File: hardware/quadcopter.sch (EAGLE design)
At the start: 92 parts, among them J1 HEADER-4POS-0.1IN-FEMALE-SMD-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, J2 HEADER-10POSTH-254X10, J3 HEADER-4POS-0.1IN-FEMALE, J4 AVR_SPI_PRG_6-SMD, M1 MOTOR_PADS_GND-MOLEX-SMD, M2 MOTOR_PADS_GND-MOLEX-SMD, M3 MOTOR_PADS_GND-MOLEX-SMD, M4 MOTOR_PADS_GND-MOLEX-SMD, Q1 N-MOSFET-SI2302DS, Q10 N-MOSFET-SI2302DS, Q11 N-MOSFET-SI2302DS, Q12 N-MOSFET-SI2302DS, Q2 N-MOSFET-SI2302DS, Q3 N-MOSFET-SI2302DS, Q4 N-MOSFET-SI2302DS, Q5 N-MOSFET-SI2302DS, Q6 N-MOSFET-SI2302DS, Q7 N-MOSFET-SI2302DS, Q8 N-MOSFET-SI2302DS, Q9 N-MOSFET-SI2302DS, SW1 PUSHBUTTON_-4.5X4.5, U1 ATMEGA128RFA1, U2 IMU_LSM9DS1-LSM9DS1, Y1 CRYSTAL5X3

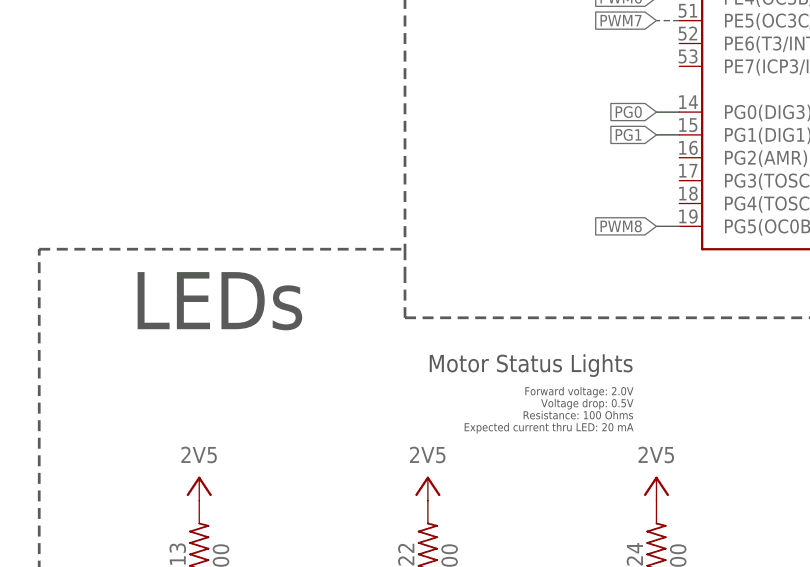
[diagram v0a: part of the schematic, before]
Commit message: Fixed 2V5 net on both sides of R15
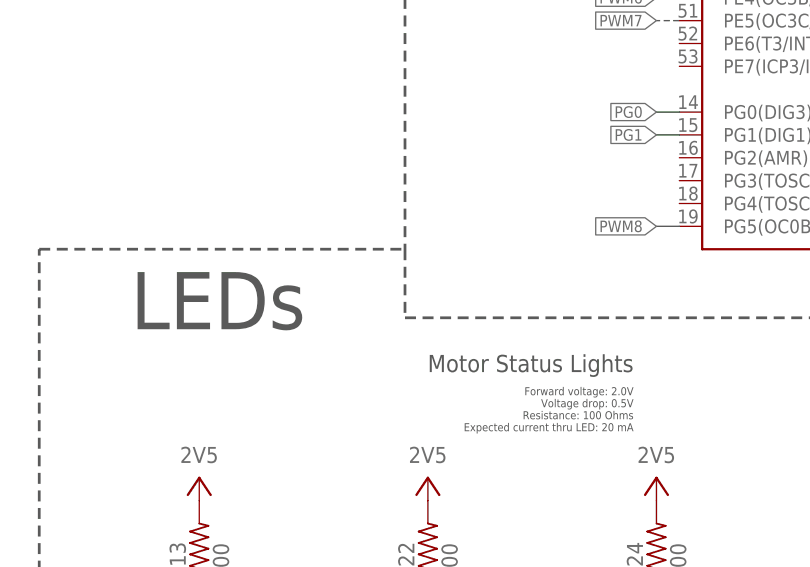
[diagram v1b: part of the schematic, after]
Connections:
- new net N$33: D12.A, R15.1
- net 2V5: no longer D12.A, R15.1
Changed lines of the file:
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@@
 <text x="332.74" y="116.84" size="7.62" layer="97">Power Supply</text>
 <wire x1="154.94" y1="274.32" x2="154.94" y2="137.16" width="0.3048" layer="97" style="longdash"/>
-<wire x1="154.94" y1="134.62" x2="154.94" y2="129.54" width="0.3048" layer="97" style="longdash"/>
+<wire x1="154.94" y1="137.16" x2="154.94" y2="129.54" width="0.3048" layer="97" style="longdash"/>
 <wire x1="154.94" y1="129.54" x2="327.66" y2="129.54" width="0.3048" layer="97" style="longdash"/>
 <text x="205.74" y="261.62" size="7.62" layer="97">Microcontroller</text>
@@
 <wire x1="114.3" y1="58.42" x2="114.3" y2="137.16" width="0.3048" layer="97" style="longdash"/>
 <wire x1="114.3" y1="137.16" x2="154.94" y2="137.16" width="0.3048" layer="97" style="longdash"/>
-<wire x1="154.94" y1="137.16" x2="154.94" y2="134.62" width="0.3048" layer="97" style="longdash"/>
 <wire x1="261.62" y1="60.96" x2="314.96" y2="60.96" width="0.1524" layer="97" style="longdash"/>
 </plain>
@@
 </segment>
 <segment>
-<pinref part="D12" gate="G$1" pin="A"/>
 <pinref part="R15" gate="G$1" pin="2"/>
-<pinref part="R15" gate="G$1" pin="1"/>
 <pinref part="R8" gate="G$1" pin="2"/>
 <wire x1="238.76" y1="111.76" x2="243.84" y2="111.76" width="0.1524" layer="91"/>
@@
 </segment>
 </net>
+<net name="N$33" class="0">
+<segment>
+<pinref part="D12" gate="G$1" pin="A"/>
+<pinref part="R15" gate="G$1" pin="1"/>
+</segment>
+</net>

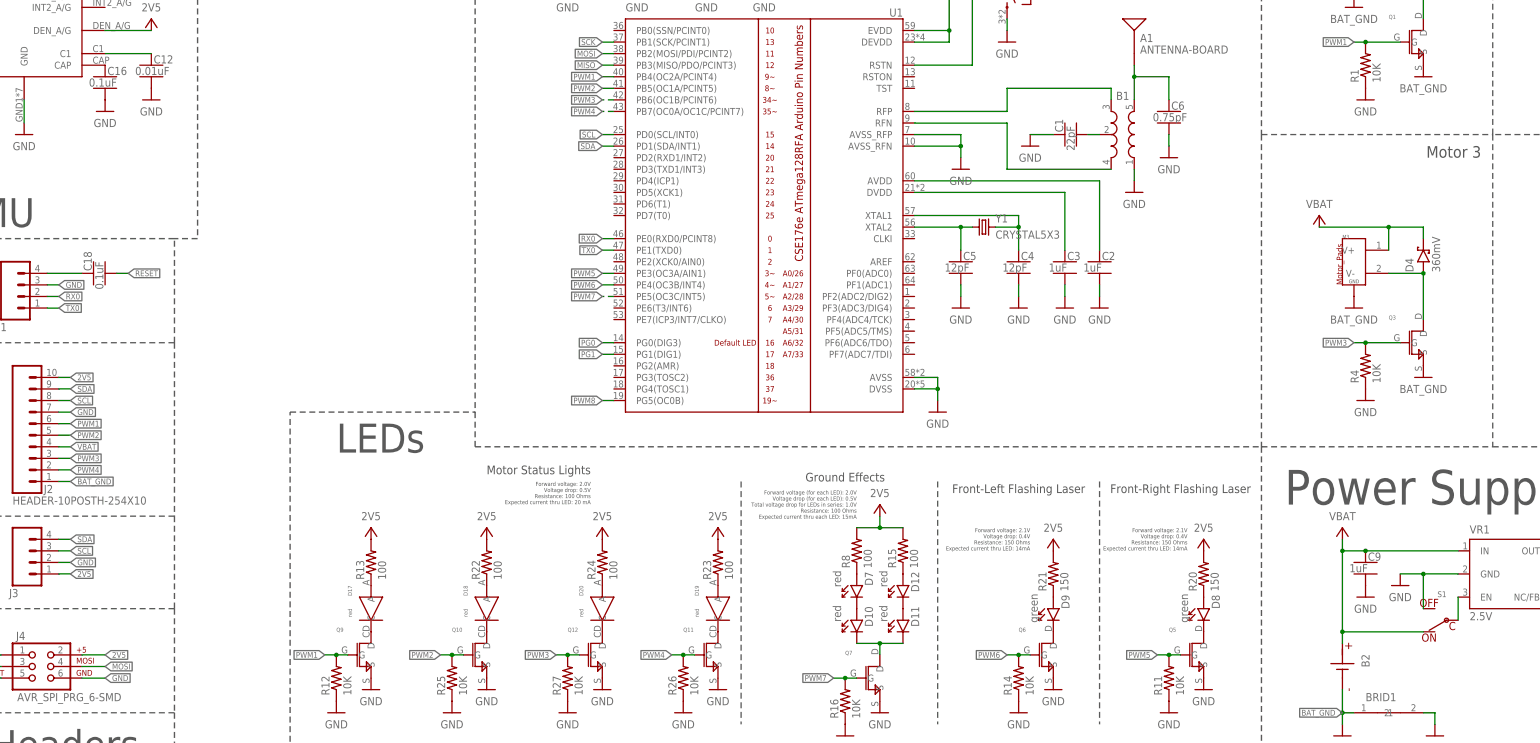
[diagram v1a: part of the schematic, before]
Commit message: Wired some pins to GND and switch to BAT_GND for eaglint
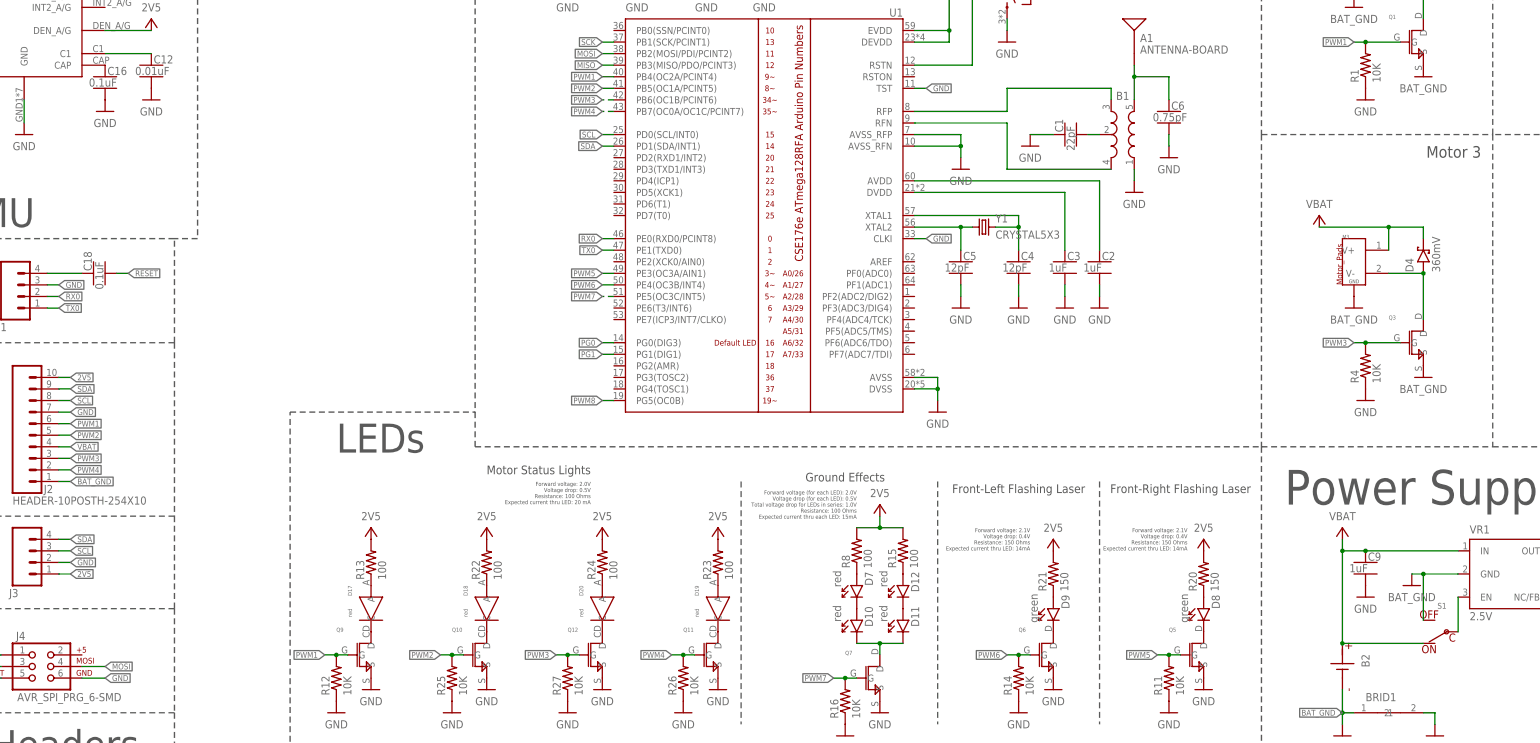
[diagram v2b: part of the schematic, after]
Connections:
- net 2V5: no longer J4.2
- net BAT_GND: now also S1.OFF, VR1.GND
- net GND: now also U1.CLKI, U1.TST; no longer S1.OFF, VR1.GND
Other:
- moved on the sheet: S1
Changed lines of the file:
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@@
 <part name="A1" library="quadparts_prebuilt_2022" library_urn="urn:adsk.wipprod:fs.file:vf.VudH_-qgS-enOFMGlZoxrw" deviceset="ANTENNA" device="-BOARD"/>
 <part name="VR1" library="quadparts_prebuilt_2022" library_urn="urn:adsk.wipprod:fs.file:vf.VudH_-qgS-enOFMGlZoxrw" deviceset="TPS73633-DBVT" device="2.5V" value="2.5V"/>
-<part name="GND27" library="quadparts_prebuilt_2022" library_urn="urn:adsk.wipprod:fs.file:vf.VudH_-qgS-enOFMGlZoxrw" deviceset="GND" device=""/>
 <part name="C9" library="quadparts_prebuilt_2022" library_urn="urn:adsk.wipprod:fs.file:vf.VudH_-qgS-enOFMGlZoxrw" deviceset="CAPACITOR-NP_" device="SMD-2012-0805_CERAMIC-1UF" value="1uF"/>
 <part name="C10" library="quadparts_prebuilt_2022" library_urn="urn:adsk.wipprod:fs.file:vf.VudH_-qgS-enOFMGlZoxrw" deviceset="CAPACITOR-NP_" device="SMD-2012-0805_CERAMIC-1UF" value="1uF"/>
@@
 <part name="R18" library="quadparts_prebuilt_2022" library_urn="urn:adsk.wipprod:fs.file:vf.VudH_-qgS-enOFMGlZoxrw" deviceset="RESISTOR_" device="SMD-2012-0805-100" value="100"/>
 <part name="P+21" library="quadparts_prebuilt_2022" library_urn="urn:adsk.wipprod:fs.file:vf.VudH_-qgS-enOFMGlZoxrw" deviceset="2V5" device=""/>
+<part name="GND27" library="quadparts_prebuilt_2022" library_urn="urn:adsk.wipprod:fs.file:vf.VudH_-qgS-enOFMGlZoxrw" deviceset="BAT_GND" device=""/>
 </parts>
 <sheets>
@@
 <attribute name="NAME" x="373.38" y="110.49" size="1.778" layer="95"/>
 </instance>
-<instance part="GND27" gate="1" x="358.14" y="99.06" smashed="yes">
-<attribute name="VALUE" x="358.14" y="96.52" size="1.778" layer="96" align="center"/>
-</instance>
 <instance part="C9" gate="G$1" x="350.52" y="104.14" smashed="yes">
 <attribute name="VALUE" x="346.964" y="101.981" size="1.778" layer="96"/>
@@
 <attribute name="NAME" x="401.828" y="101.981" size="1.778" layer="95"/>
 </instance>
-<instance part="S1" gate="G$1" x="365.76" y="91.44" smashed="yes" rot="R180">
-<attribute name="NAME" x="368.3" y="97.79" size="1.27" layer="95" rot="R180"/>
+<instance part="S1" gate="G$1" x="365.76" y="88.9" smashed="yes" rot="R180">
+<attribute name="NAME" x="368.3" y="95.25" size="1.27" layer="95" rot="R180"/>
 </instance>
 <instance part="GND31" gate="1" x="350.52" y="96.52" smashed="yes">
@@
 <instance part="P+21" gate="G$1" x="314.96" y="45.72" smashed="yes">
 <attribute name="VALUE" x="314.96" y="48.26" size="1.778" layer="96" rot="R180" align="center"/>
+</instance>
+<instance part="GND27" gate="1" x="360.68" y="99.06" smashed="yes">
+<attribute name="VALUE" x="360.68" y="96.52" size="1.778" layer="96" align="center"/>
 </instance>
 </instances>
@@
 </segment>
 <segment>
-<wire x1="370.84" y1="101.6" x2="363.22" y2="101.6" width="0.1524" layer="91"/>
-<wire x1="363.22" y1="101.6" x2="358.14" y2="101.6" width="0.1524" layer="91"/>
-<pinref part="VR1" gate="G$1" pin="GND"/>
-<pinref part="GND27" gate="1" pin="GND"/>
-<pinref part="S1" gate="G$1" pin="OFF"/>
-<wire x1="363.22" y1="93.98" x2="363.22" y2="101.6" width="0.1524" layer="91"/>
-<junction x="363.22" y="101.6"/>
-</segment>
-<segment>
 <pinref part="C9" gate="G$1" pin="2"/>
 <pinref part="GND31" gate="1" pin="GND"/>
@@
 <pinref part="Q8" gate="G$1" pin="S"/>
 <pinref part="GND44" gate="1" pin="GND"/>
+</segment>
+<segment>
+<pinref part="U1" gate="G$1" pin="TST"/>
+<wire x1="251.46" y1="208.28" x2="254" y2="208.28" width="0.1524" layer="91"/>
+<label x="254" y="208.28" size="1.27" layer="95" xref="yes"/>
+</segment>
+<segment>
+<pinref part="U1" gate="G$1" pin="CLKI"/>
+<wire x1="254" y1="175.26" x2="251.46" y2="175.26" width="0.1524" layer="91"/>
+<label x="254" y="175.26" size="1.27" layer="95" xref="yes"/>
 </segment>
 </net>
@@
 <pinref part="Q4" gate="G$1" pin="S"/>
 </segment>
+<segment>
+<wire x1="370.84" y1="101.6" x2="363.22" y2="101.6" width="0.1524" layer="91"/>
+<wire x1="363.22" y1="101.6" x2="360.68" y2="101.6" width="0.1524" layer="91"/>
+<pinref part="VR1" gate="G$1" pin="GND"/>
+<pinref part="S1" gate="G$1" pin="OFF"/>
+<wire x1="363.22" y1="91.44" x2="363.22" y2="101.6" width="0.1524" layer="91"/>
+<pinref part="GND27" gate="1" pin="BAT_GND"/>
+<junction x="363.22" y="101.6"/>
+</segment>
 </net>
 <net name="VBAT" class="0">
@@
 </segment>
 <segment>
-<wire x1="363.22" y1="88.9" x2="345.44" y2="88.9" width="0.1524" layer="91"/>
+<wire x1="363.22" y1="86.36" x2="345.44" y2="86.36" width="0.1524" layer="91"/>
 <wire x1="345.44" y1="109.22" x2="345.44" y2="106.68" width="0.1524" layer="91"/>
-<wire x1="345.44" y1="106.68" x2="345.44" y2="88.9" width="0.1524" layer="91"/>
-<wire x1="345.44" y1="88.9" x2="345.44" y2="86.36" width="0.1524" layer="91"/>
+<wire x1="345.44" y1="106.68" x2="345.44" y2="86.36" width="0.1524" layer="91"/>
 <pinref part="S1" gate="G$1" pin="ON"/>
 <pinref part="P+17" gate="VCC" pin="VBAT"/>
 <pinref part="B2" gate="G$1" pin="P"/>
-<junction x="345.44" y="88.9"/>
 <pinref part="VR1" gate="G$1" pin="IN"/>
 <wire x1="370.84" y1="106.68" x2="350.52" y2="106.68" width="0.1524" layer="91"/>
 <pinref part="C9" gate="G$1" pin="1"/>
 <wire x1="350.52" y1="106.68" x2="345.44" y2="106.68" width="0.1524" layer="91"/>
+<junction x="345.44" y="86.36"/>
+<junction x="345.44" y="106.68"/>
 <junction x="350.52" y="106.68"/>
-<junction x="345.44" y="106.68"/>
 </segment>
 <segment>
@@
 <wire x1="63.5" y1="101.6" x2="66.04" y2="101.6" width="0.1524" layer="91"/>
 <label x="66.04" y="101.6" size="1.27" layer="95" xref="yes"/>
-</segment>
-<segment>
-<pinref part="J4" gate="G$1" pin="2"/>
-<wire x1="68.58" y1="83.82" x2="73.66" y2="83.82" width="0.1524" layer="91"/>
-<label x="73.66" y="83.82" size="1.27" layer="95" xref="yes"/>
 </segment>
 <segment>
@@
 <pinref part="VR1" gate="G$1" pin="EN"/>
 <pinref part="S1" gate="G$1" pin="C"/>
-<wire x1="370.84" y1="91.44" x2="370.84" y2="96.52" width="0.1524" layer="91"/>
-</segment>
-</net>
+<wire x1="370.84" y1="88.9" x2="370.84" y2="96.52" width="0.1524" layer="91"/>
+</segment>
+</net>

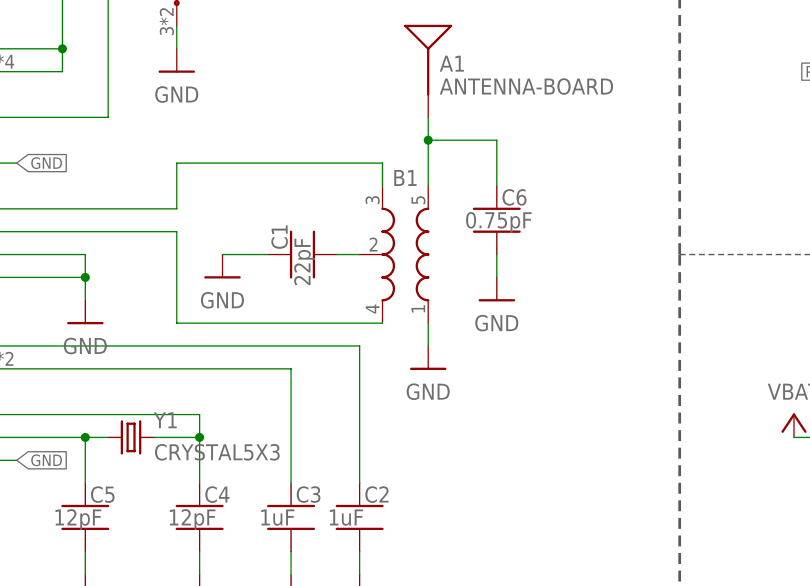
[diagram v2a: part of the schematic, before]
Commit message: Reorient balun
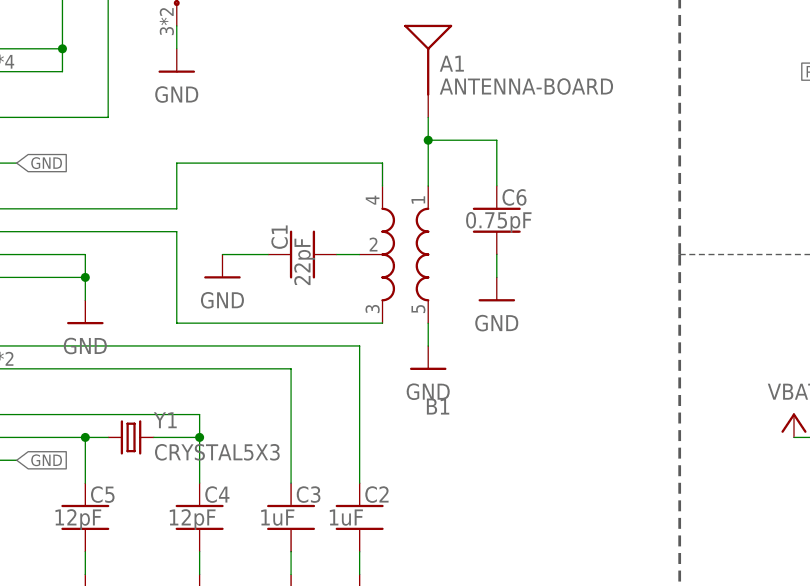
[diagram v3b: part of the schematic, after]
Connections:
- net GND: now also B1.GND@5; no longer B1.IN
- net N$12: now also B1.OUT1; no longer B1.OUT2
- net N$14: now also B1.IN; no longer B1.GND@5
- net N$15: now also B1.OUT2; no longer B1.OUT1
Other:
- moved on the sheet: B1
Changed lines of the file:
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@@
 <part name="P+16" library="quadparts_prebuilt_2022" library_urn="urn:adsk.wipprod:fs.file:vf.VudH_-qgS-enOFMGlZoxrw" deviceset="2V5" device=""/>
 <part name="U1" library="quadparts_prebuilt_2022" library_urn="urn:adsk.wipprod:fs.file:vf.VudH_-qgS-enOFMGlZoxrw" deviceset="ATMEGA128RFA1" device=""/>
-<part name="B1" library="quadparts_prebuilt_2022" library_urn="urn:adsk.wipprod:fs.file:vf.VudH_-qgS-enOFMGlZoxrw" deviceset="BALUN" device="0805"/>
 <part name="C1" library="quadparts_prebuilt_2022" library_urn="urn:adsk.wipprod:fs.file:vf.VudH_-qgS-enOFMGlZoxrw" deviceset="CAPACITOR-NP_" device="SMD-2012-0805_CERAMIC-22PF" value="22pF"/>
 <part name="C2" library="quadparts_prebuilt_2022" library_urn="urn:adsk.wipprod:fs.file:vf.VudH_-qgS-enOFMGlZoxrw" deviceset="CAPACITOR-NP_" device="SMD-2012-0805_CERAMIC-1UF" value="1uF"/>
@@
 <part name="P+21" library="quadparts_prebuilt_2022" library_urn="urn:adsk.wipprod:fs.file:vf.VudH_-qgS-enOFMGlZoxrw" deviceset="2V5" device=""/>
 <part name="GND27" library="quadparts_prebuilt_2022" library_urn="urn:adsk.wipprod:fs.file:vf.VudH_-qgS-enOFMGlZoxrw" deviceset="BAT_GND" device=""/>
+<part name="B1" library="quadparts_prebuilt_2022" library_urn="urn:adsk.wipprod:fs.file:vf.VudH_-qgS-enOFMGlZoxrw" deviceset="BALUN" device="0805"/>
 </parts>
 <sheets>
@@
 <attribute name="NAME" x="248.92" y="224.028" size="1.778" layer="95" rot="MR0"/>
 </instance>
-<instance part="B1" gate="G$1" x="297.18" y="195.58" smashed="yes" rot="R180">
-<attribute name="NAME" x="297.18" y="205.74" size="1.778" layer="95" rot="R180" align="top-center"/>
-</instance>
 <instance part="C1" gate="G$1" x="284.48" y="198.12" smashed="yes" rot="R90">
 <attribute name="VALUE" x="286.639" y="194.564" size="1.778" layer="96" rot="R90"/>
@@
 <instance part="GND27" gate="1" x="360.68" y="99.06" smashed="yes">
 <attribute name="VALUE" x="360.68" y="96.52" size="1.778" layer="96" align="center"/>
+</instance>
+<instance part="B1" gate="G$1" x="297.18" y="200.66" smashed="yes" rot="MR0">
+<attribute name="NAME" x="302.26" y="180.34" size="1.778" layer="95" rot="MR0"/>
 </instance>
 </instances>
@@
 <segment>
 <wire x1="299.72" y1="187.96" x2="299.72" y2="190.5" width="0.1524" layer="91"/>
-<pinref part="B1" gate="G$1" pin="IN"/>
 <pinref part="GND18" gate="1" pin="GND"/>
+<pinref part="B1" gate="G$1" pin="GND@5"/>
 </segment>
 <segment>
@@
 <segment>
 <wire x1="292.1" y1="198.12" x2="289.56" y2="198.12" width="0.1524" layer="91"/>
+<pinref part="C1" gate="G$1" pin="2"/>
 <pinref part="B1" gate="G$1" pin="GND@2"/>
-<pinref part="C1" gate="G$1" pin="2"/>
 </segment>
 </net>
@@
 <wire x1="294.64" y1="208.28" x2="294.64" y2="205.74" width="0.1524" layer="91"/>
 <pinref part="U1" gate="G$1" pin="RFP"/>
-<pinref part="B1" gate="G$1" pin="OUT2"/>
+<pinref part="B1" gate="G$1" pin="OUT1"/>
 </segment>
 </net>
@@
 <wire x1="307.34" y1="210.82" x2="299.72" y2="210.82" width="0.1524" layer="91"/>
 <junction x="299.72" y="210.82"/>
-<pinref part="B1" gate="G$1" pin="GND@5"/>
 <pinref part="C6" gate="G$1" pin="1"/>
 <pinref part="A1" gate="G$1" pin="SIGNAL"/>
+<pinref part="B1" gate="G$1" pin="IN"/>
 </segment>
 </net>
@@
 <wire x1="271.78" y1="190.5" x2="294.64" y2="190.5" width="0.1524" layer="91"/>
 <pinref part="U1" gate="G$1" pin="RFN"/>
-<pinref part="B1" gate="G$1" pin="OUT1"/>
-</segment>
-</net>
+<pinref part="B1" gate="G$1" pin="OUT2"/>
+</segment>
+</net>
